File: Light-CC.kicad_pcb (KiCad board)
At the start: 2 copper layers, 69 x 36 mm, 69 parts, among them J1 Conn_01x02_Pin, J2 Conn_01x02_Pin, J3 Conn_01x02_Pin, J4 Conn_01x03_Male, J5 USB_C_Receptacle_USB2.0, Q1 BS870, Q2 STD7NK40Z, Q3 BS870, Q4 BC547, Q5 BC547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

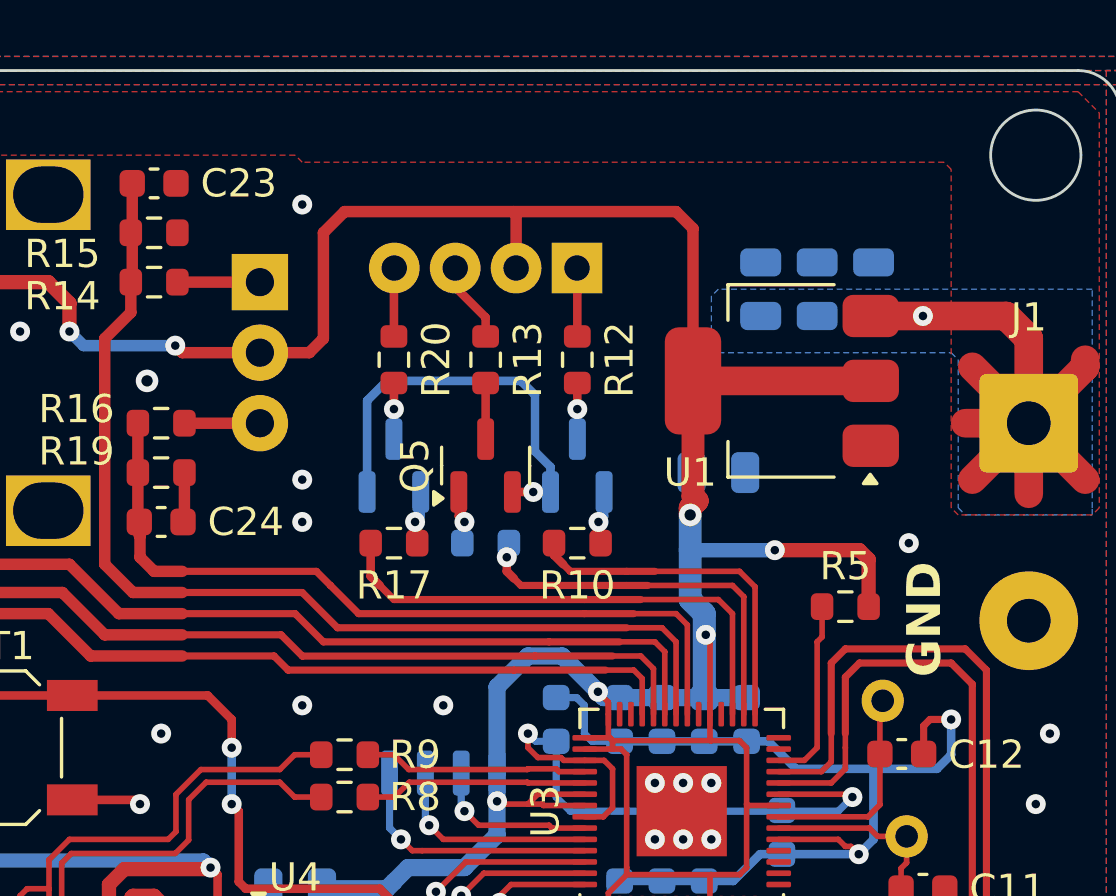
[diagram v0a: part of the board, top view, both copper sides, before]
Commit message: Pwr led added
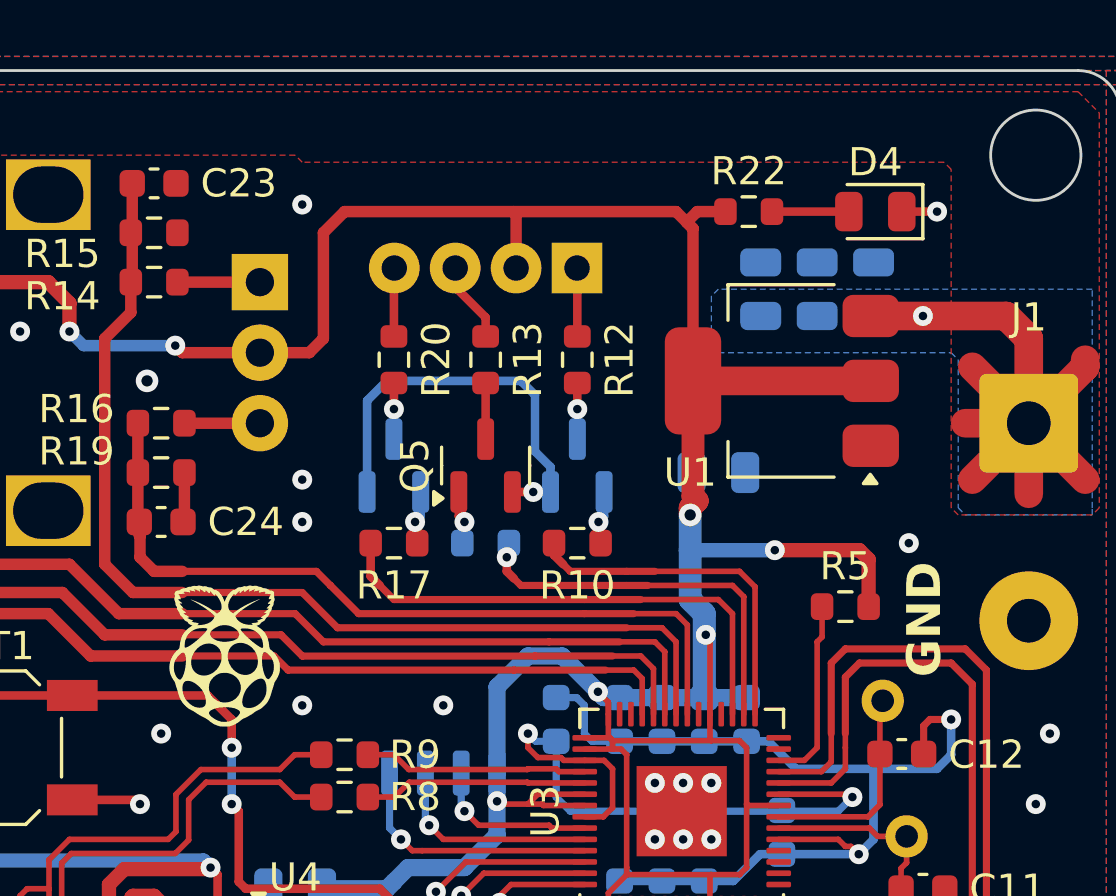
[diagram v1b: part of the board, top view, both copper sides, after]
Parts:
- added D4: LED, LED_SMD:LED_0805_2012Metric, F.Cu at (140.3, 89.0)
- added G***: LOGO, LOGO, F.Cu at (117.2, 104.8)
- added R22: 1K, Resistor_SMD:R_0603_1608Metric, F.Cu at (135.8, 89.0)
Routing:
- net Net-(D4-A): track 0.00 -> 2.72 mm
- net +3V3: track 190.7 -> 192.5 mm
- net GND: track 95.0 -> 96.3 mm, vias 38 -> 39

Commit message: Design Completed & Gerber generated
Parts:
- added G***: LOGO, LOGO, B.Cu at (110.2, 105.5)
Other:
- board text added: "Light-CC_V1"
